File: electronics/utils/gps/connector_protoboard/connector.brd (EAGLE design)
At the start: 39 x 64.1 mm, 2 parts, among them X1 87758-2016

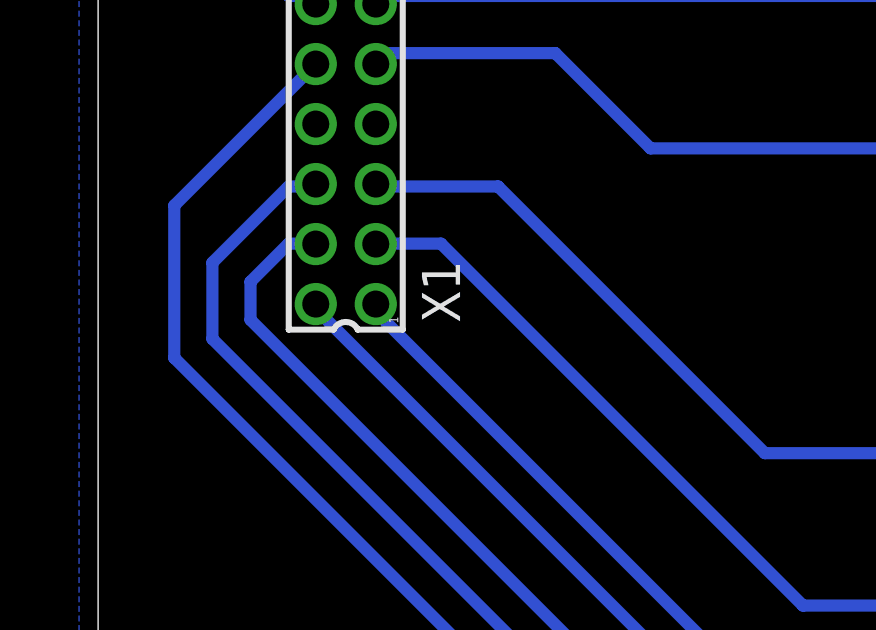
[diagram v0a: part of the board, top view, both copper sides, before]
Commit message: adicionado nota do numero 1 na placa para facilitar montagem
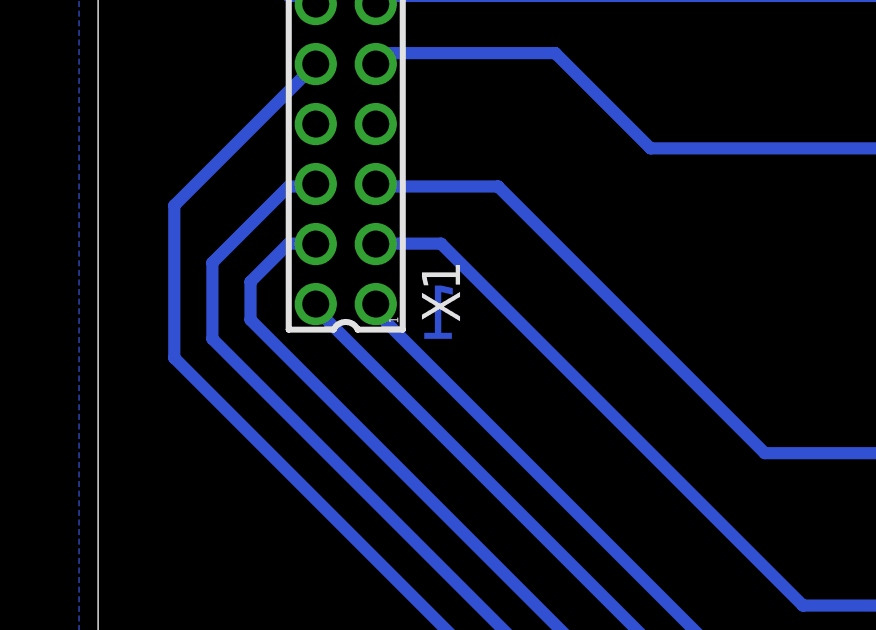
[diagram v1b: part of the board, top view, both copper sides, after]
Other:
- board text added: "1"
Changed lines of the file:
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@@
 <wire x1="40.945" y1="77.46" x2="1.905" y2="77.46" width="0" layer="20"/>
 <wire x1="1.905" y1="77.46" x2="1.905" y2="13.335" width="0" layer="20"/>
+<text x="13.97" y="35.56" size="1.778" layer="16" rot="MR0">1</text>
 </plain>
 <attributes>
